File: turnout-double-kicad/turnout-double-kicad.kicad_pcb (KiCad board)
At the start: 2 copper layers, 23 x 37 mm, 19 parts

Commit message: Turnout-double: add mounting holes clearance.
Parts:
- turned H1 to 270 degrees

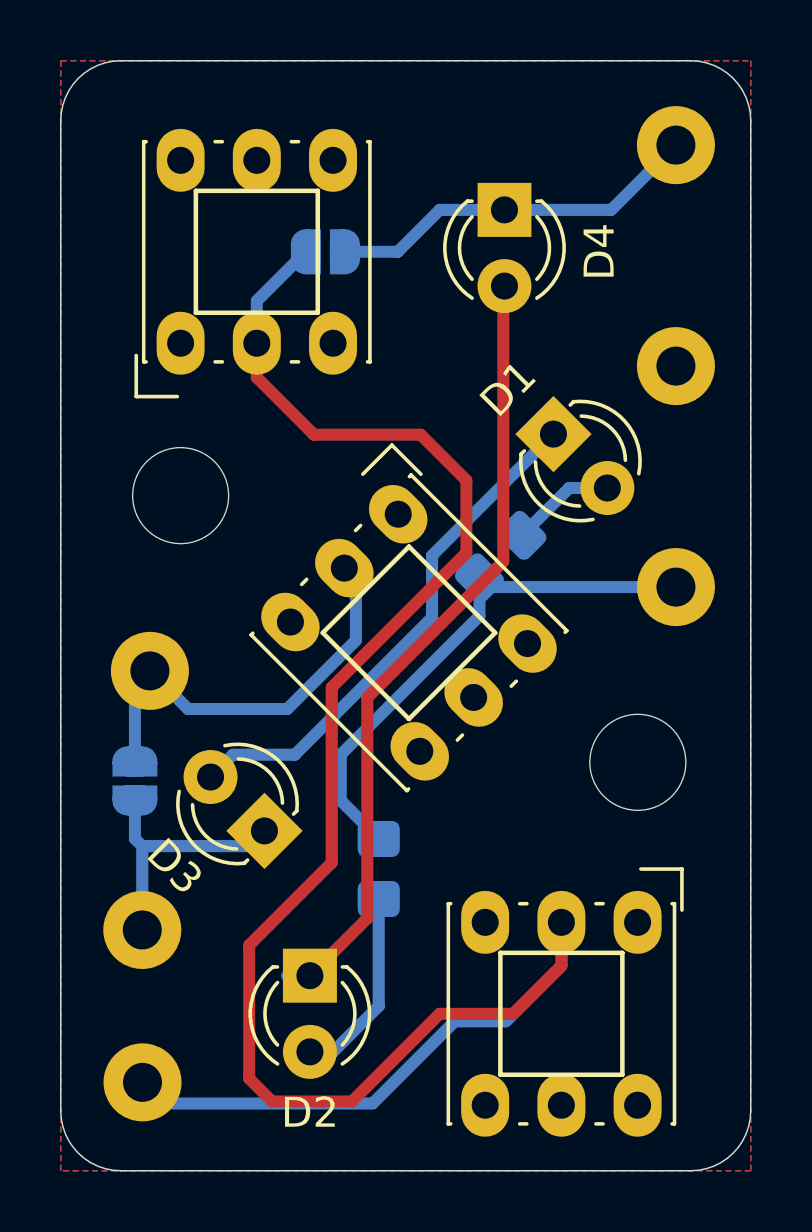
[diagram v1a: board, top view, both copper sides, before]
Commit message: Turnout-double: allow both side placement.
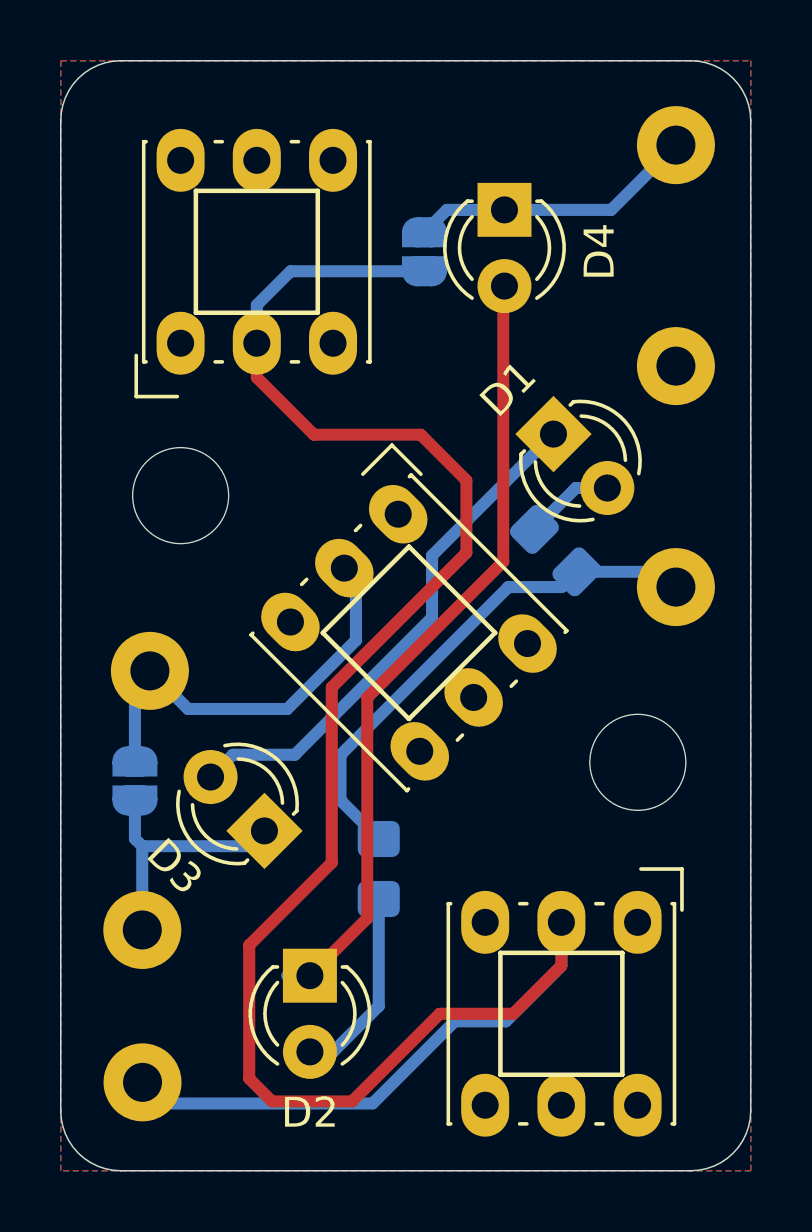
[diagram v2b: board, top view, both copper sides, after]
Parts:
- moved JP1 3.30 mm to (103.1, 23.4), turned to 270 degrees
- moved R1 1.84 mm to (107.5, 33.3), turned to 135 degrees
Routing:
- net Net-(JP1-Pad2): track 67.9 -> 71.5 mm
- net Net-(D4-Pad1): track 12.5 -> 10.2 mm
- net VCC: track 17.8 -> 17.2 mm
- net Net-(D1-Pad2): track 3.50 -> 3.00 mm

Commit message: Turnout-double: dubplicate parts.
To allow mirror placement on panel.
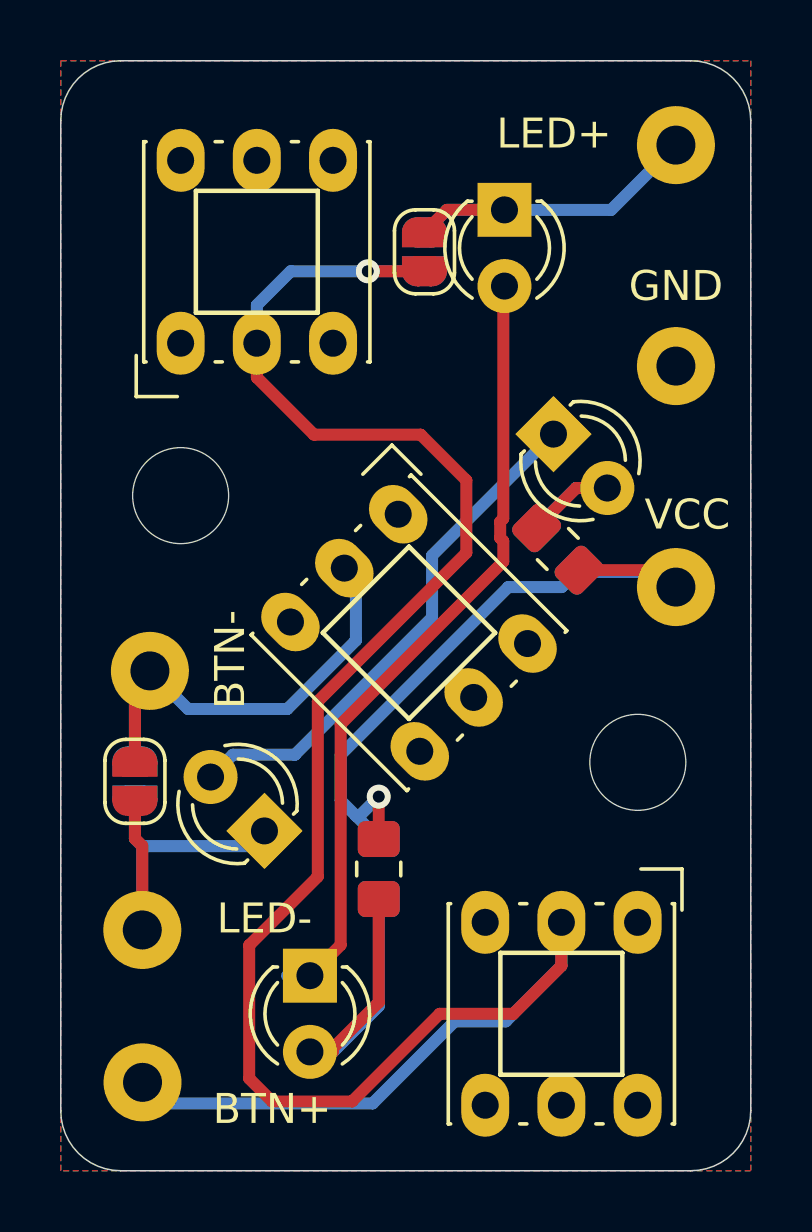
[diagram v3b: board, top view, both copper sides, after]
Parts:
- added JP3: SJ, Jumper:SolderJumper-2_P1.3mm_Open_RoundedPad1.0x1.5mm, F.Cu at (103.1, 23.4)
- added JP4: SJ, Jumper:SolderJumper-2_P1.3mm_Open_RoundedPad1.0x1.5mm, F.Cu at (93.5, 41.0)
- added R1: 1k, Resistor_SMD:R_0805_2012Metric_Pad1.20x1.40mm_HandSolder, F.Cu at (101.6, 43.9)
- added R3: 1k, Resistor_SMD:R_0805_2012Metric_Pad1.20x1.40mm_HandSolder, F.Cu at (107.6, 33.3)
- moved R4 0.09 mm to (107.6, 33.3)
- renumbered D2 to D1, D1 to D2, D4 to D3, D3 to D4, R1 to R4
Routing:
- net Net-(D1-Pad2): track 6.50 -> 13.7 mm
- net VCC: track 17.2 -> 23.1 mm, vias 0 -> 1
- net Net-(D4-Pad1): track 8.70 -> 13.1 mm
- net Net-(JP2-Pad2): track 14.3 -> 17.5 mm
- net Net-(D3-Pad1): track 10.2 -> 13.2 mm
- net Net-(D2-Pad2): track 3.00 -> 5.91 mm
- net Net-(JP1-Pad2): track 71.5 -> 73.3 mm, vias 0 -> 1

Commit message: turnout-double: migrate to KiCad 6.
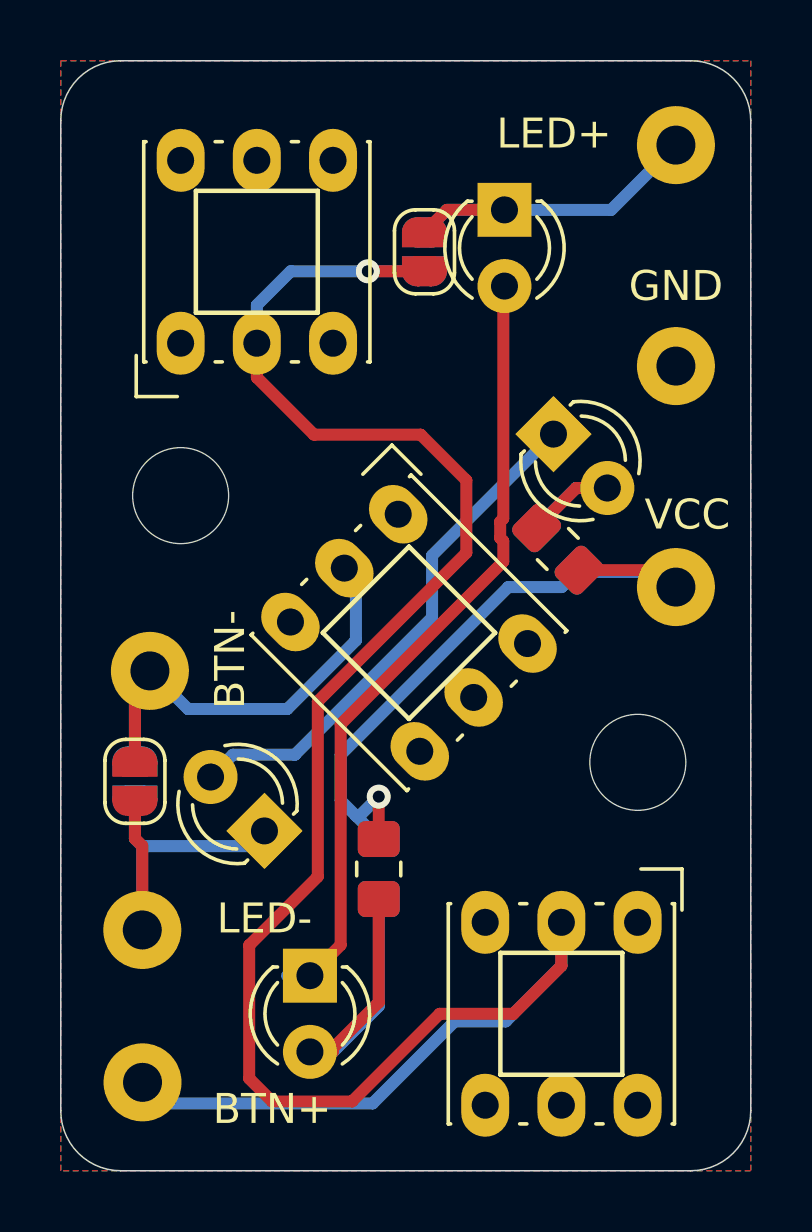
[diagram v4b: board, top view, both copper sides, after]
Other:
- net class Default removed

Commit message: turnout-double: add wires for reversed placing.
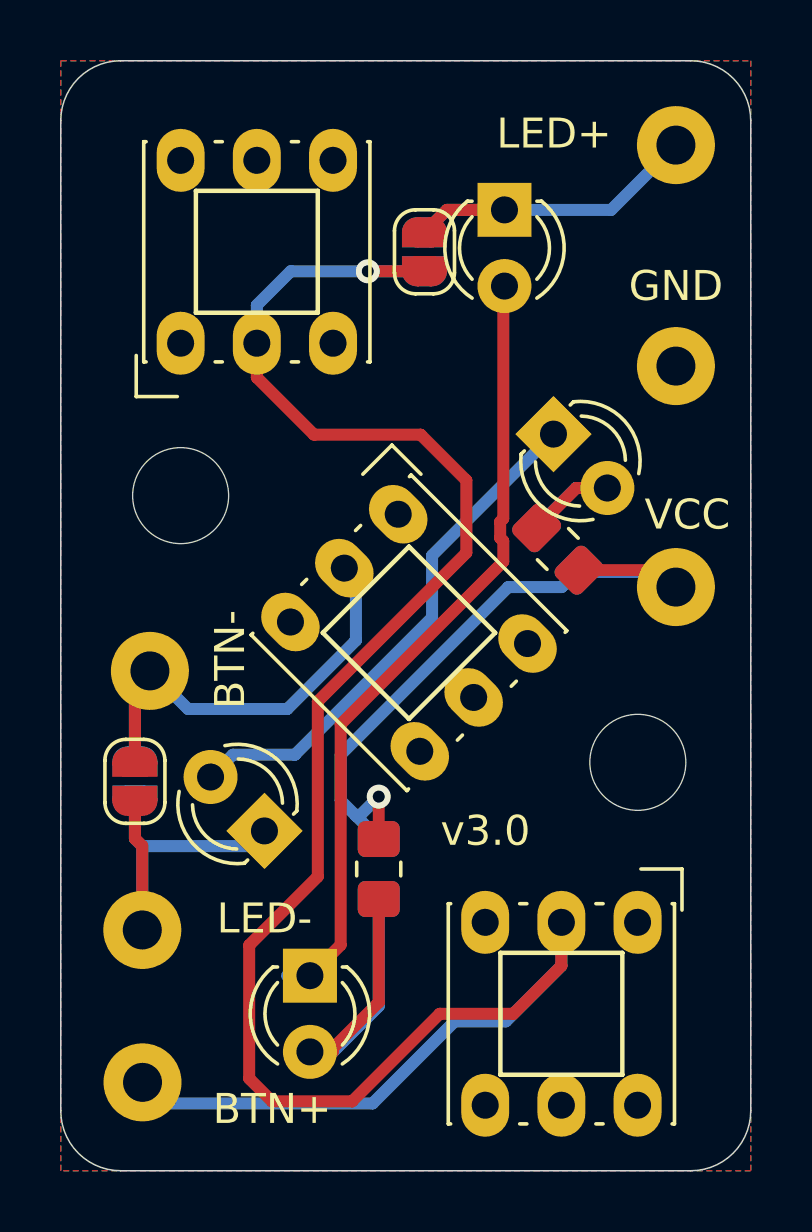
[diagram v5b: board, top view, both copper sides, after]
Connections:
- SWMINUS1 pad 1: (no net) -> GND
- SWMINUS1 pad 4: (no net) -> unconnected-(SWMINUS1-Pad4)
- SWMINUS1 pad 5: (no net) -> unconnected-(SWMINUS1-Pad5)
- SWMINUS1 pad 6: (no net) -> unconnected-(SWMINUS1-Pad6)
- SWPLUS1 pad 1: (no net) -> GND
- SWPLUS1 pad 4: (no net) -> unconnected-(SWPLUS1-Pad4)
- SWPLUS1 pad 5: (no net) -> unconnected-(SWPLUS1-Pad5)
- SWPLUS1 pad 6: (no net) -> unconnected-(SWPLUS1-Pad6)
- SWPLUS2 pad 1: (no net) -> unconnected-(SWPLUS2-Pad1)
- SWPLUS2 pad 4: (no net) -> unconnected-(SWPLUS2-Pad4)
- SWPLUS2 pad 5: (no net) -> unconnected-(SWPLUS2-Pad5)
- SWPLUS2 pad 6: (no net) -> unconnected-(SWPLUS2-Pad6)
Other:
- board text added: "v3.0"

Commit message: turnout-double: add author & version to silkscreen.
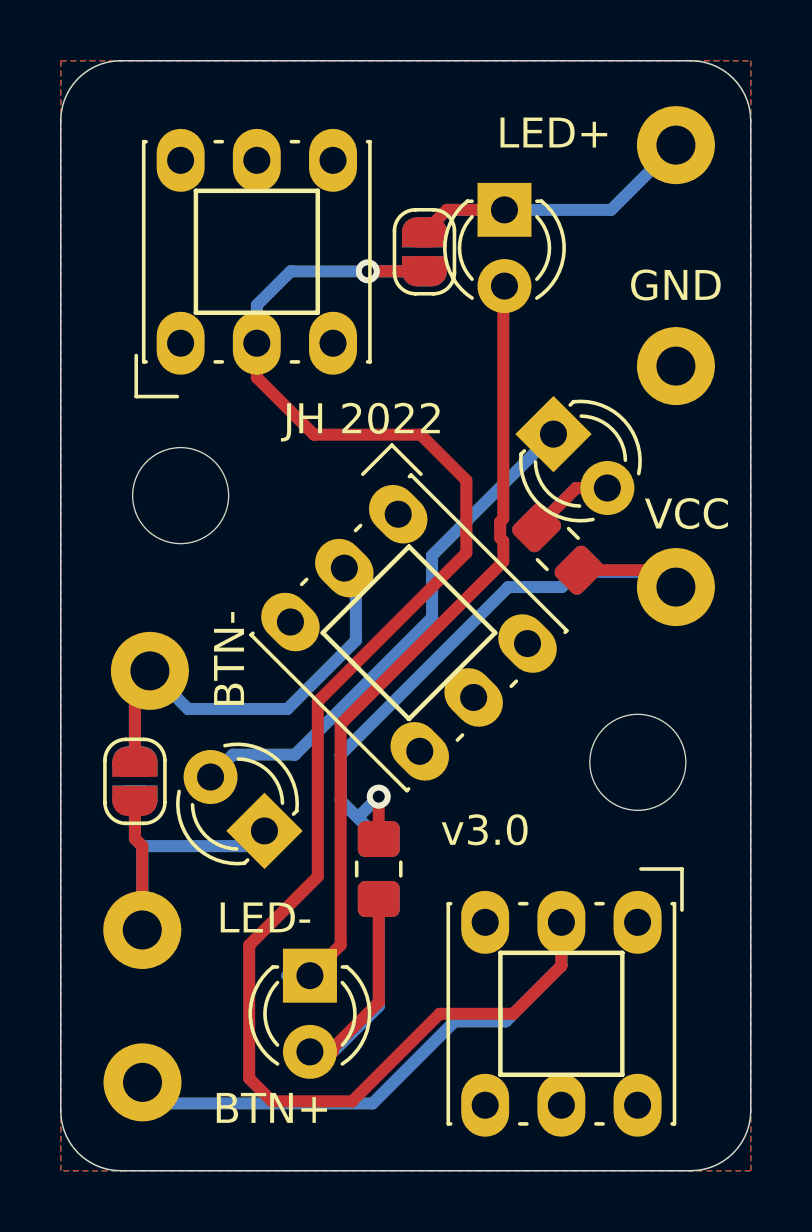
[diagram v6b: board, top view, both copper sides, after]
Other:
- board text added: "JH 2022"
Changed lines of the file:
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@@
+    (effects (font (size 1 1) (thickness 0.15)) (justify mirror))
+  )
+  (gr_text "JH 2022" (at 101.346 29.21) (layer "B.SilkS")
     (effects (font (size 1 1) (thickness 0.15)) (justify mirror))
   )
@@
   )
   (gr_text "GND" (at 111.506 24.384 180) (layer "B.SilkS")
+    (effects (font (size 1 1) (thickness 0.15)) (justify mirror))
+  )
+  (gr_text "v3.0" (at 105.156 42.672) (layer "B.SilkS")
     (effects (font (size 1 1) (thickness 0.15)) (justify mirror))
   )
@@
     (effects (font (size 1 1) (thickness 0.15)))
   )
+  (gr_text "JH 2022" (at 101.092 28.956) (layer "F.SilkS")
+    (effects (font (size 1 1) (thickness 0.15)))
+  )
